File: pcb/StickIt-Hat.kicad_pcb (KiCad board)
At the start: 2 copper layers, 65 x 56 mm, 39 parts, among them CON1 BARREL_JACK, J1 XuLA_IO_HDR, J3 JSHORTNORMAL, J4 JSHORTNORMAL, J5 JSHORTNORMAL, SW1 SW_PUSH, U1 NCV1117, U2 CAT24C32

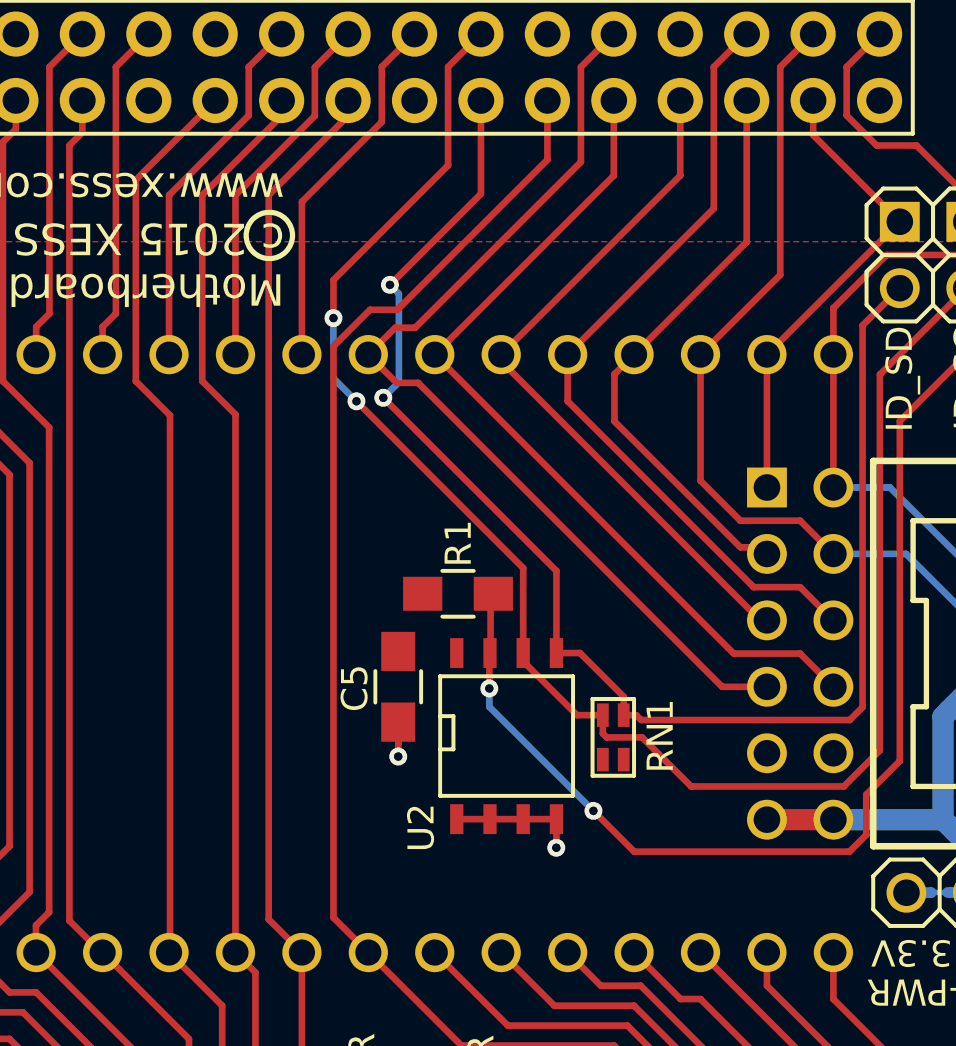
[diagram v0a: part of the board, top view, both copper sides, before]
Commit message: Changed name to StickIt-Hat. Also restored and locked some silkscreen-only components that were removed by reimporting the netlist.
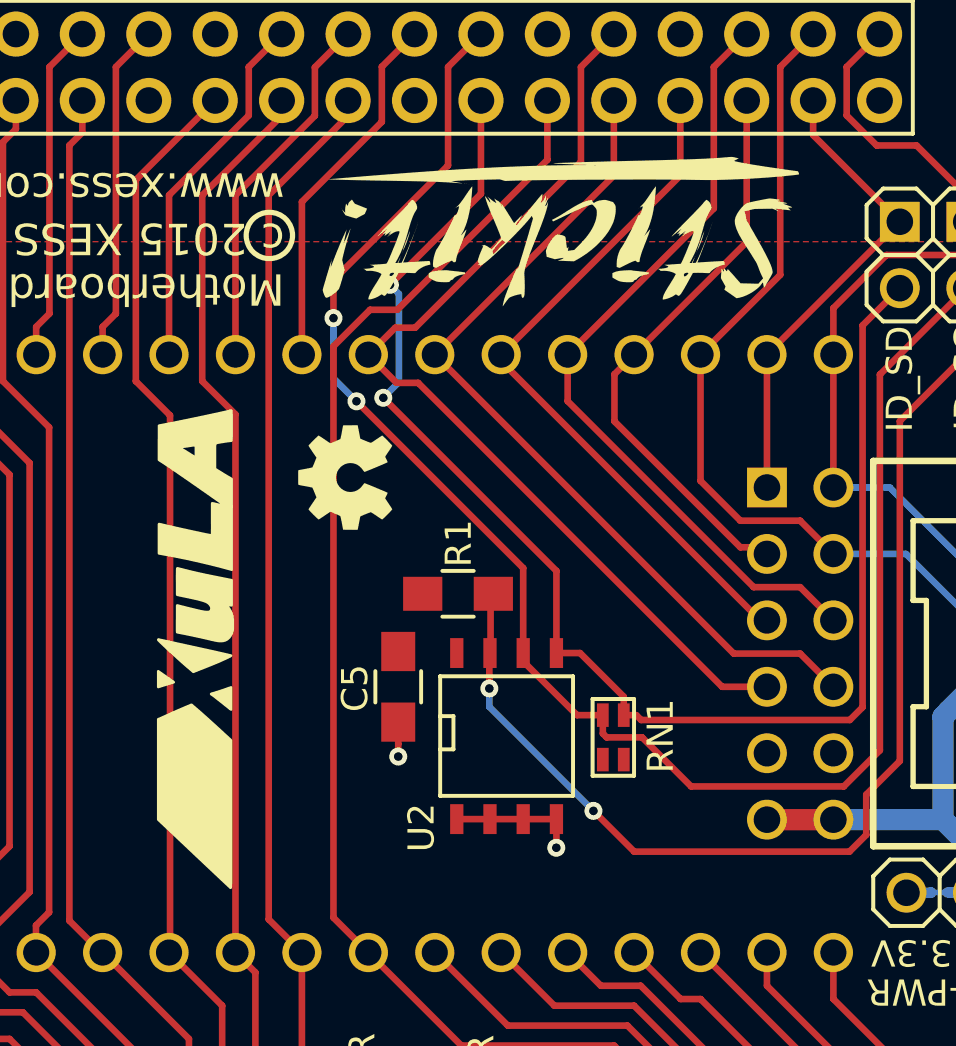
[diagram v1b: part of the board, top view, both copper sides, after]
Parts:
- added ?: , XESS Logos:stickit_logo_18mm, F.Cu at (44.5, 10.3)
- added ?: , XESS Logos:oshw_logo_4mm, F.Cu at (36.2, 19.7)
- added G***: LOGO, XESS Logos:LOGO-XULA-18x3, F.Cu at (30.5, 26.0)
- moved ? 1.28 mm to (32.4, 10.2)
